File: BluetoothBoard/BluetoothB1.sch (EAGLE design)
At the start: 5 parts, among them U1 SPBTLE-RF

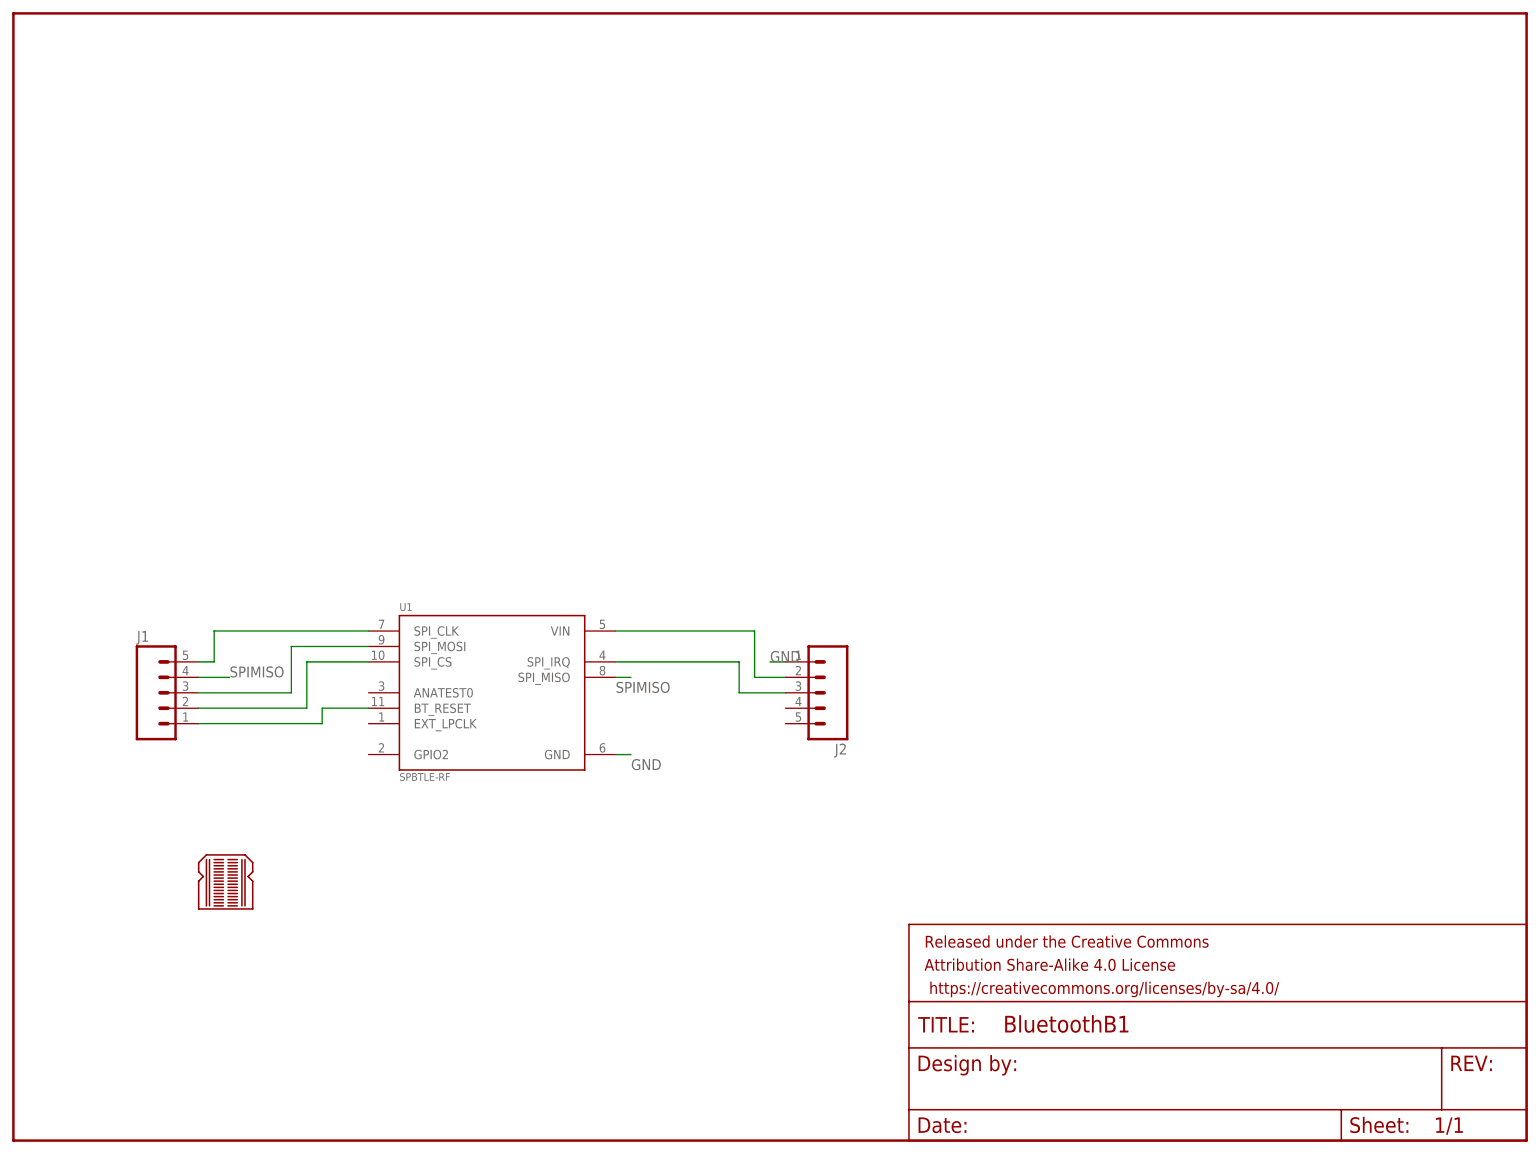
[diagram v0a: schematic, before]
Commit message: created complete LSM6DS3 implementation + configured Bluetooth to be printed
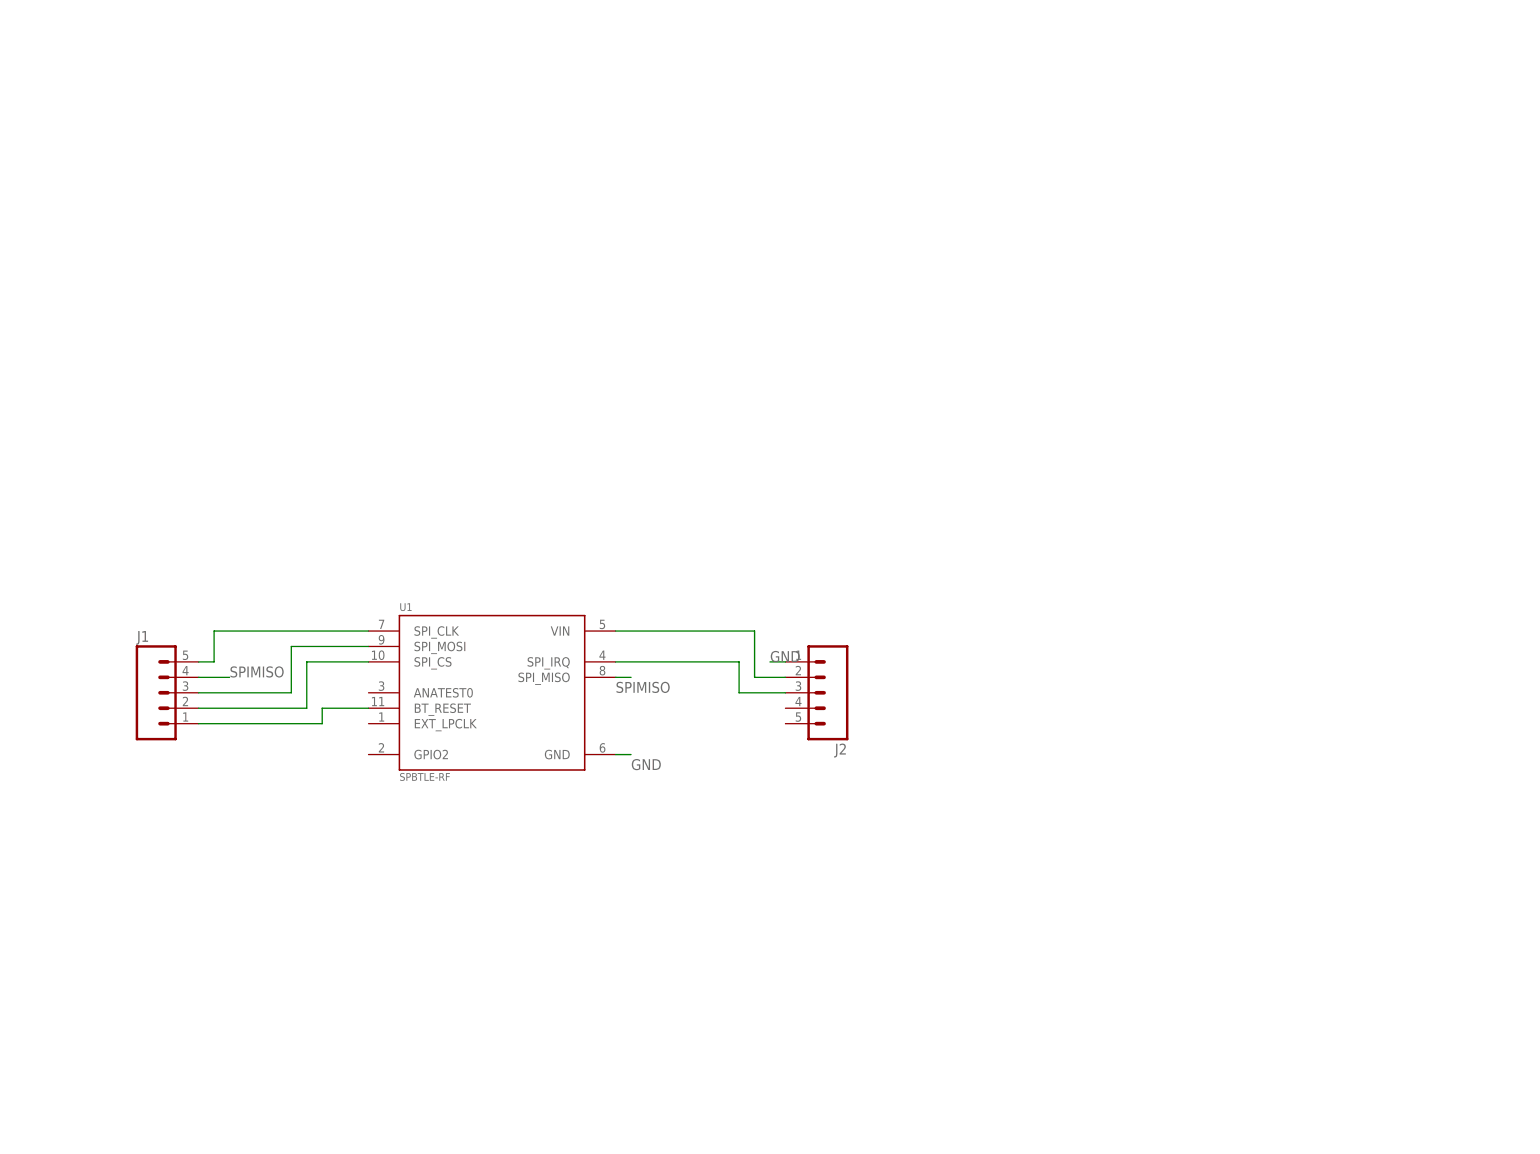
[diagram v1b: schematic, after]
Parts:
- removed FRAME1: FRAME-LETTER, SparkFun-Aesthetics:FRAME-LETTER
- removed LOGO1: BREADBOARD_PATTERN, SparkFun-Aesthetics:BREADBOARD_PATTERN
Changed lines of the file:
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@@
 </classes>
 <parts>
-<part name="FRAME1" library="SparkFun-Aesthetics" deviceset="FRAME-LETTER" device=""/>
 <part name="U1" library="SPBTLE-RF" deviceset="SPBTLE-RF" device=""/>
-<part name="LOGO1" library="SparkFun-Aesthetics" deviceset="BREADBOARD_PATTERN" device=""/>
 <part name="J1" library="SparkFun-Connectors" deviceset="M05" device="PTH"/>
 <part name="J2" library="SparkFun-Connectors" deviceset="M05" device="PTH"/>
@@
 </plain>
 <instances>
-<instance part="FRAME1" gate="G$1" x="0" y="0"/>
-<instance part="FRAME1" gate="V" x="147.32" y="0"/>
 <instance part="U1" gate="G$1" x="78.74" y="73.66"/>
-<instance part="LOGO1" gate="G$1" x="30.48" y="38.1"/>
 <instance part="J1" gate="G$1" x="22.86" y="73.66"/>
 <instance part="J2" gate="G$1" x="134.62" y="73.66" rot="R180"/>
